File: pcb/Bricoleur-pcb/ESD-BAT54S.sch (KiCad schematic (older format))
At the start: 1 part

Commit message: PCB…
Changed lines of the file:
@@
 $Descr A4 11693 8268
 encoding utf-8
-Sheet 5 18
+Sheet 3 18
 Title ""
 Date ""
@@
 AR Path="/5BEE7FFD/5BEC0258/5BB71F8A" Ref="D19"  Part="1"
 AR Path="/5BEE7FFD/5BEC025B/5BB71F8A" Ref="D20"  Part="1"
-F 0 "D8" V 5804 3037 50  0000 L CNN
+F 0 "D14" V 5804 3037 50  0000 L CNN
 F 1 "BAT54S" V 5895 3037 50  0000 L CNN
 F 2 "Package_TO_SOT_SMD:SOT-23" H 5925 3075 50  0001 L CNN

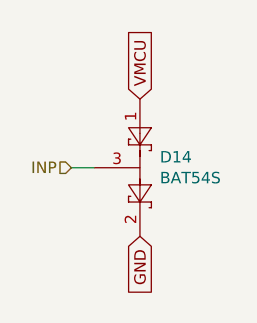
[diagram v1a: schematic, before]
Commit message: Narrowed down component placement, continued routing
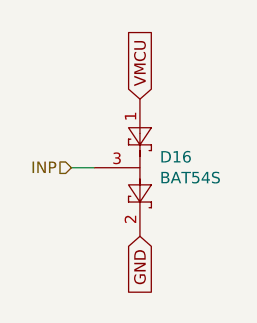
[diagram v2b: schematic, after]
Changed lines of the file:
@@
 $Descr A4 11693 8268
 encoding utf-8
-Sheet 3 18
+Sheet 13 18
 Title ""
 Date ""
@@
 AR Path="/5BEE7FFD/5BEC0258/5BB71F8A" Ref="D19"  Part="1"
 AR Path="/5BEE7FFD/5BEC025B/5BB71F8A" Ref="D20"  Part="1"
-F 0 "D14" V 5804 3037 50  0000 L CNN
+F 0 "D16" V 5804 3037 50  0000 L CNN
 F 1 "BAT54S" V 5895 3037 50  0000 L CNN
 F 2 "Package_TO_SOT_SMD:SOT-23" H 5925 3075 50  0001 L CNN

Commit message: Big fookup.
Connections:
- net GND: now also D8.1; no longer D8.2
- net VMCU: now also D8.2; no longer D8.1
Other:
- moved on the sheet: D19
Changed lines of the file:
@@
 $Descr A4 11693 8268
 encoding utf-8
-Sheet 13 18
+Sheet 17 18
 Title ""
 Date ""
@@
 Comment4 ""
 $EndDescr
-Text HLabel 5550 2950 0    50   Input ~ 0
+Text HLabel 6050 2950 2    50   Input ~ 0
 INP
 $Comp
@@
 AR Path="/5BEE7FFD/5BEC0258/5BB71F8A" Ref="D19"  Part="1"
 AR Path="/5BEE7FFD/5BEC025B/5BB71F8A" Ref="D20"  Part="1"
-F 0 "D16" V 5804 3037 50  0000 L CNN
+F 0 "D19" V 5804 3037 50  0000 L CNN
 F 1 "BAT54S" V 5895 3037 50  0000 L CNN
 F 2 "Package_TO_SOT_SMD:SOT-23" H 5925 3075 50  0001 L CNN
 F 3 "https://www.diodes.com/assets/Datasheets/ds11005.pdf" H 5730 2950 50  0001 C CNN
 	1    5850 2950
-	0    1    1    0
+	0    -1   -1   0
 $EndComp
-Wire Wire Line
-	5650 2950 5550 2950
 Text GLabel 5850 3250 3    50   Input ~ 0
 GND

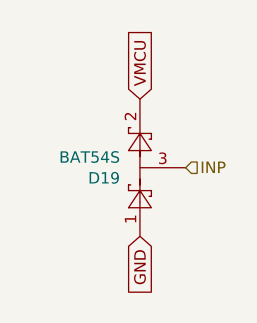
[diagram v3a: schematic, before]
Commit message: Cleanup, labeling, schematic size reduction
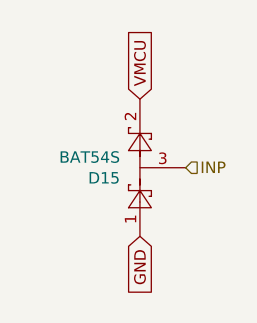
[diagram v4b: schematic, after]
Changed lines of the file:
@@
 $Descr A4 11693 8268
 encoding utf-8
-Sheet 17 18
+Sheet 8 10
 Title ""
 Date ""
@@
 AR Path="/5BEE7FFD/5BEC0258/5BB71F8A" Ref="D19"  Part="1"
 AR Path="/5BEE7FFD/5BEC025B/5BB71F8A" Ref="D20"  Part="1"
-F 0 "D19" V 5804 3037 50  0000 L CNN
+F 0 "D15" V 5804 3037 50  0000 L CNN
 F 1 "BAT54S" V 5895 3037 50  0000 L CNN
 F 2 "Package_TO_SOT_SMD:SOT-23" H 5925 3075 50  0001 L CNN
